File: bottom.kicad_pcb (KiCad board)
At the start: 2 copper layers, 49.5 x 147.2 mm, 56 parts, among them J10 105162-0001, J2 USB_B_Micro, J6 Conn_01x04, J7 Conn_01x02, J8 Conn_01x02, J9 Conn_01x02, Q1 PN2222A, Q2 Q_NMOS_GSD, Q3 PN2222A, U1 ESP32-WROOM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

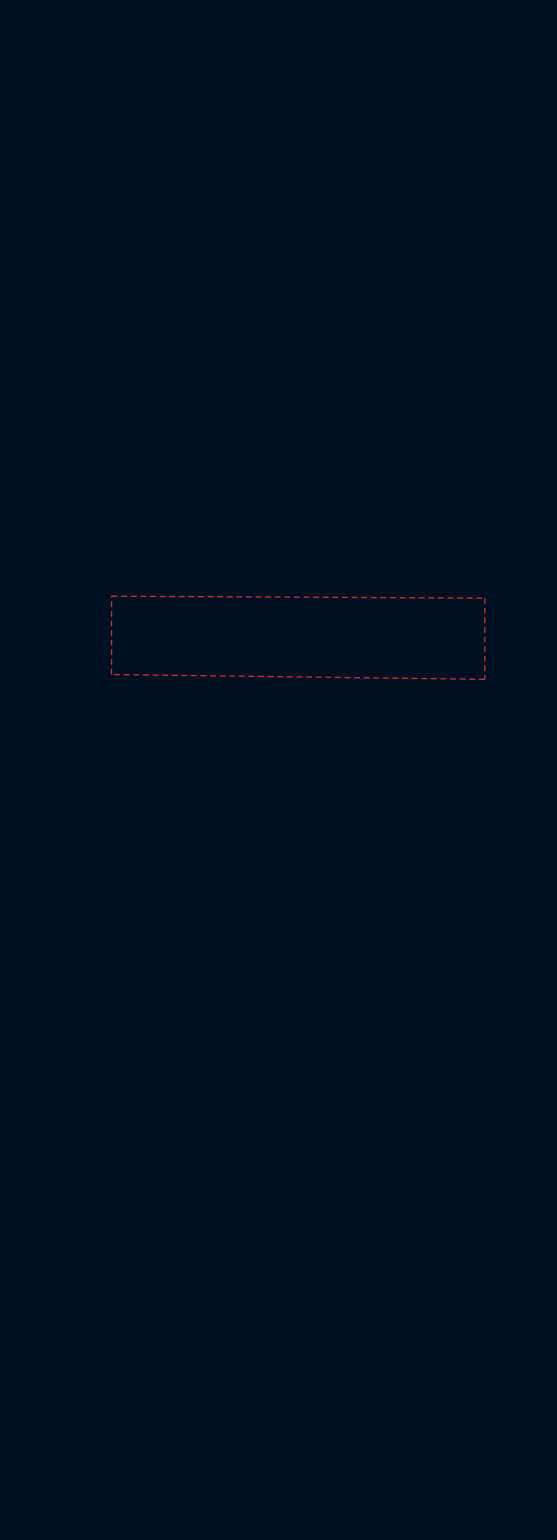
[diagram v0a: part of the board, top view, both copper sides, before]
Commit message: removed designators, more cosmetic fixes
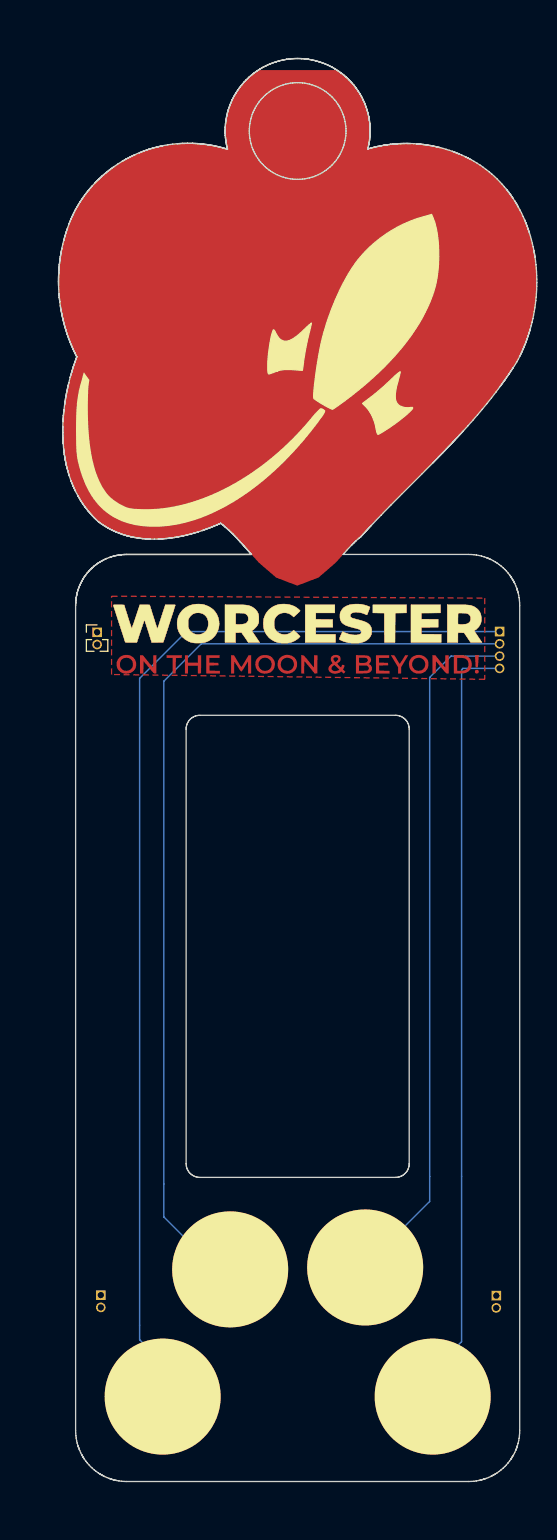
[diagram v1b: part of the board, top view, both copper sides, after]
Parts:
- added J1: Conn_01x04, Connector_PinHeader_1.27mm:PinHeader_1x04_P1.27mm_Vertical, B.Cu at (222.2, 86.0)
- added J3: Conn_01x02, Connector_PinHeader_1.27mm:PinHeader_1x02_P1.27mm_Vertical, B.Cu at (181.0, 154.6)
- added J4: Conn_01x02, Connector_PinHeader_1.27mm:PinHeader_1x02_P1.27mm_Vertical, B.Cu at (221.9, 154.6)
- added J5: Conn_01x02, Connector_PinHeader_1.27mm:PinHeader_1x02_P1.27mm_Vertical, F.Cu at (180.6, 86.0)
- added svg2mod: G***, moonbadge:artwork, F.Cu at (200.8, 100.3)
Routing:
- net T7: track 43.9 -> 152.4 mm, vias 0 -> 1
- net T6: track 43.6 -> 138.7 mm, vias 0 -> 1
- net T4: track 38.9 -> 113.5 mm, vias 0 -> 1
- net T5: track 41.4 -> 108.0 mm, vias 0 -> 1
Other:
- outline, holes or cut-outs redrawn
- board text added: "MoonBadge.github.io"
- board text added: "Moonbadge Rev.1 Alex Camilo"

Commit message: more cosmetic updates. dont check in gerbers
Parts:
- removed J1: Conn_01x04, Connector_PinHeader_1.27mm:PinHeader_1x04_P1.27mm_Vertical
- removed J3, J4, J5: Conn_01x02, Connector_PinHeader_1.27mm:PinHeader_1x02_P1.27mm_Vertical
- removed the svg2mod at (200.8, 100.3)
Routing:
- removed copper zone on F.Cu, net (none)
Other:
- outline, holes or cut-outs redrawn
